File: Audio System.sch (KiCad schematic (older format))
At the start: 41 parts

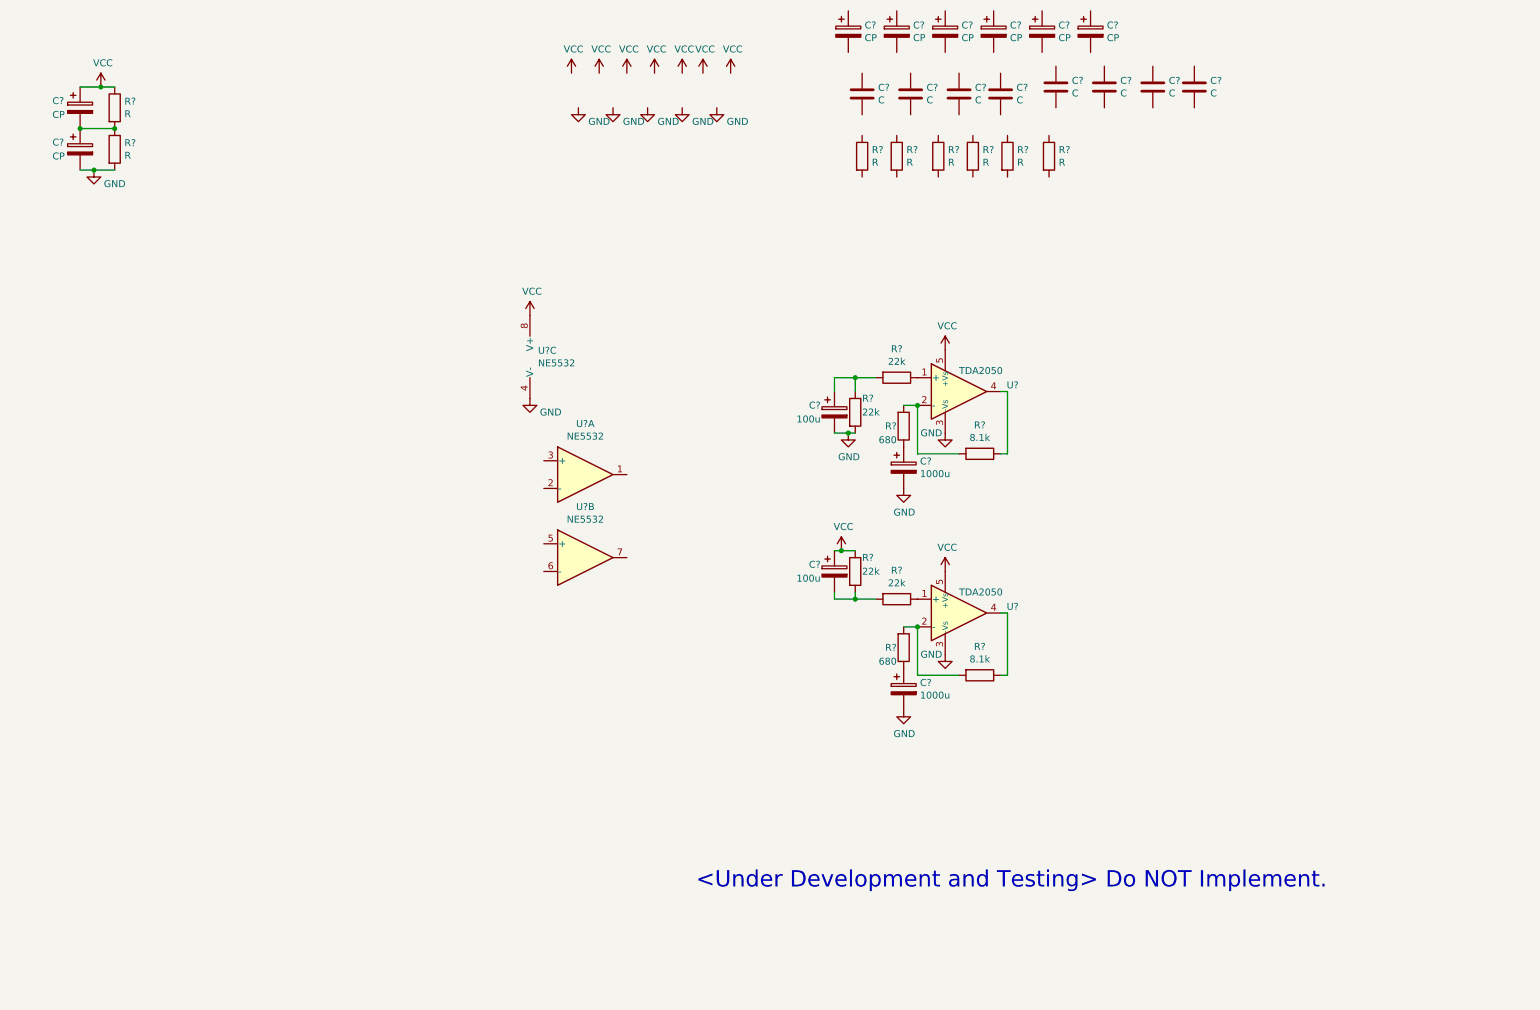
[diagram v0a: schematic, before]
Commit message: 0.2b
Power Amplifier Test 1 Complete
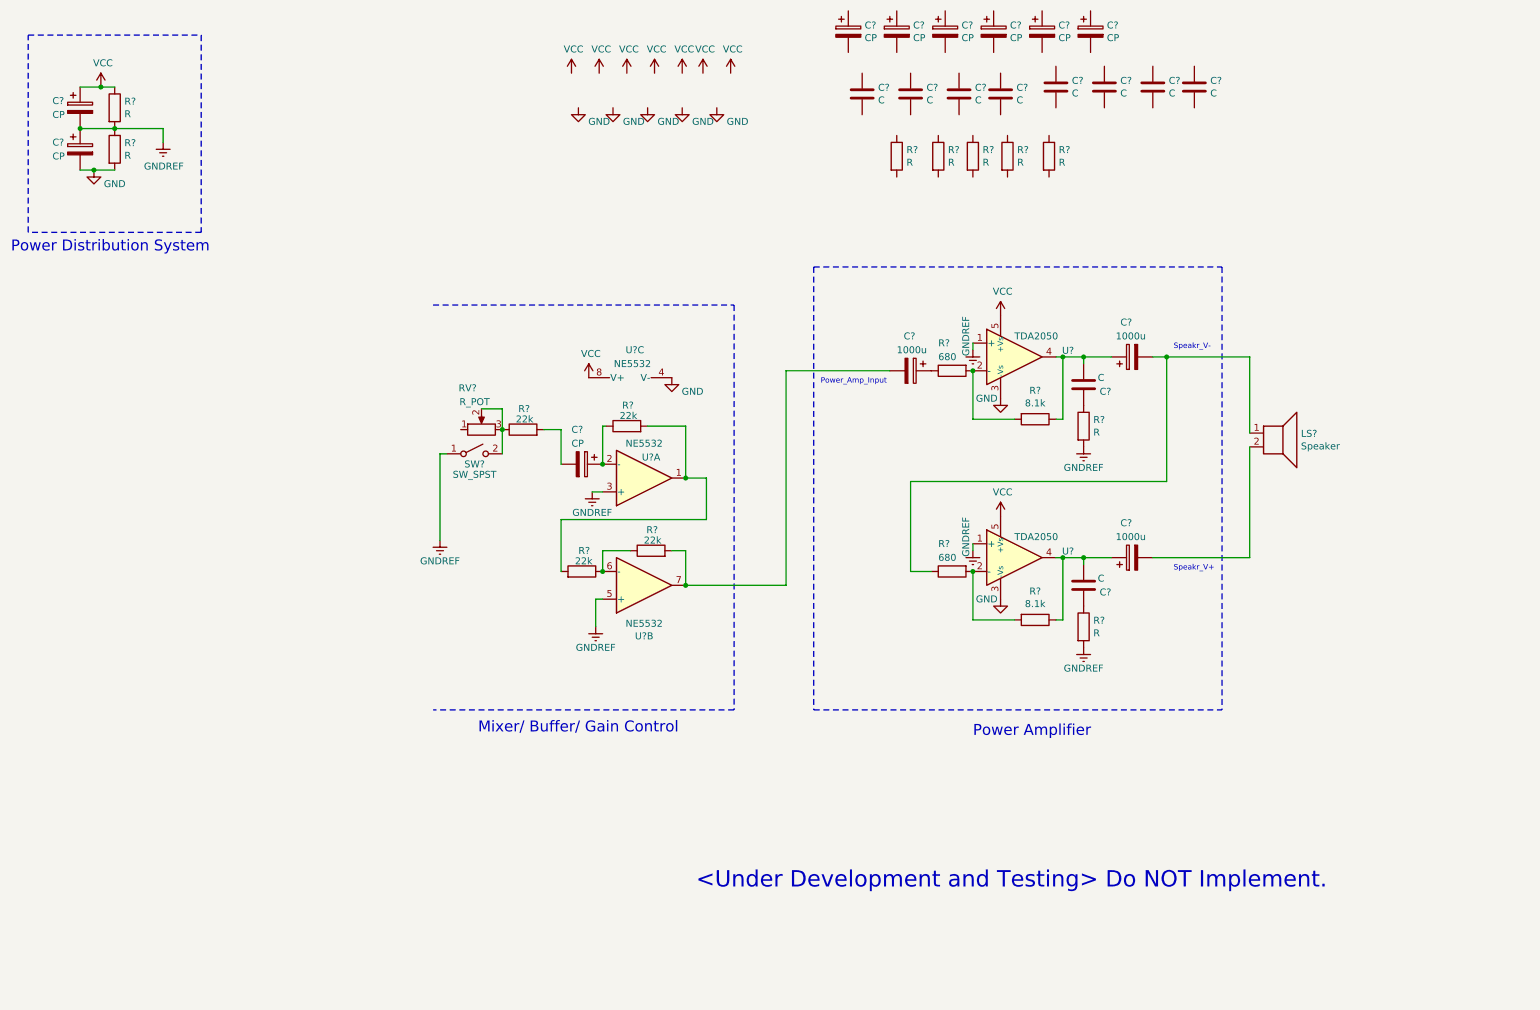
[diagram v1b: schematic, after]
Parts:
- removed C? (x2): 100u, symbol Device:CP
- removed C?: 1000u, symbol Device:CP
- removed R? (x4): 22k, symbol Device:R
- removed R?: 8.1k, symbol Device:R
- removed R?: 680, symbol Device:R
- removed U?: TDA2050, Package_TO_SOT_THT:TO-220-5_P3.4x3.7mm_StaggerOdd_Lead3.8mm_Vertical, symbol Amplifier_Audio:TDA2050
- added C? (x2): C, symbol Device:C
- added C? (x2): 1000u, symbol Device:CP
- added C?: CP, symbol Device:CP
- added LS?: Speaker, symbol Device:Speaker
- added R? (x2): R, symbol Device:R
- added R?: 8.1k, symbol Device:R
- added R?: 680, symbol Device:R
- added R? (x3): 22k, symbol Device:R
- added RV?: R_POT, symbol Device:R_POT
- added SW?: SW_SPST, symbol Switch:SW_SPST
- added U?: TDA2050, Package_TO_SOT_THT:TO-220-5_P3.4x3.7mm_StaggerOdd_Lead3.8mm_Vertical, symbol Amplifier_Audio:TDA2050
- R?: value R -> 22k
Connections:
- net GND: now also U?.3 (-Vs); no longer C?.2
- net VCC: now also U?.5 (+Vs)
- net GNDREF: now reaches U?.1 (+)
- net GNDREF: now also C?.1, C?.2, R?.1, R?.2, U?.3 (+), U?.5 (+), R?.2, R?.2, SW?.1 (A), U?.1 (+)
- net at R?.1, U?.4: now also C?.1, C?.2
- net at R?.1: now also U?.6 (-), R?.1
- net at R?.2: now also U?.1, R?.2
- net at U?.2 (-): now also C?.1, R?.1
- net at U?.7: now also C?.2, R?.2
- new net: C?.1, R?.1 (x2)
- new net: C?.2, LS?.1, R?.1
- new net: R?.2, R?.2, U?.2 (-)
- new net: C?.1, C?.2, R?.1, U?.4
- new net: C?.2, LS?.2
- new net: R?.1, RV?.2, RV?.3, SW?.2 (B)
- new net: C?.2, R?.2
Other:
- note added: "Mixer/ Buffer/ Gain Control"
- note added: "Power Amplifier"
- note added: "Power Distribution System"
- note added: "Power_Amp_Input"
- note added: "Speakr_V+"
- note added: "Speakr_V-"
- moved on the sheet: C?, R?, U?, U?A, U?B, U?C

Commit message: 0.3b
Input sources Preamp layout. Test Pending.
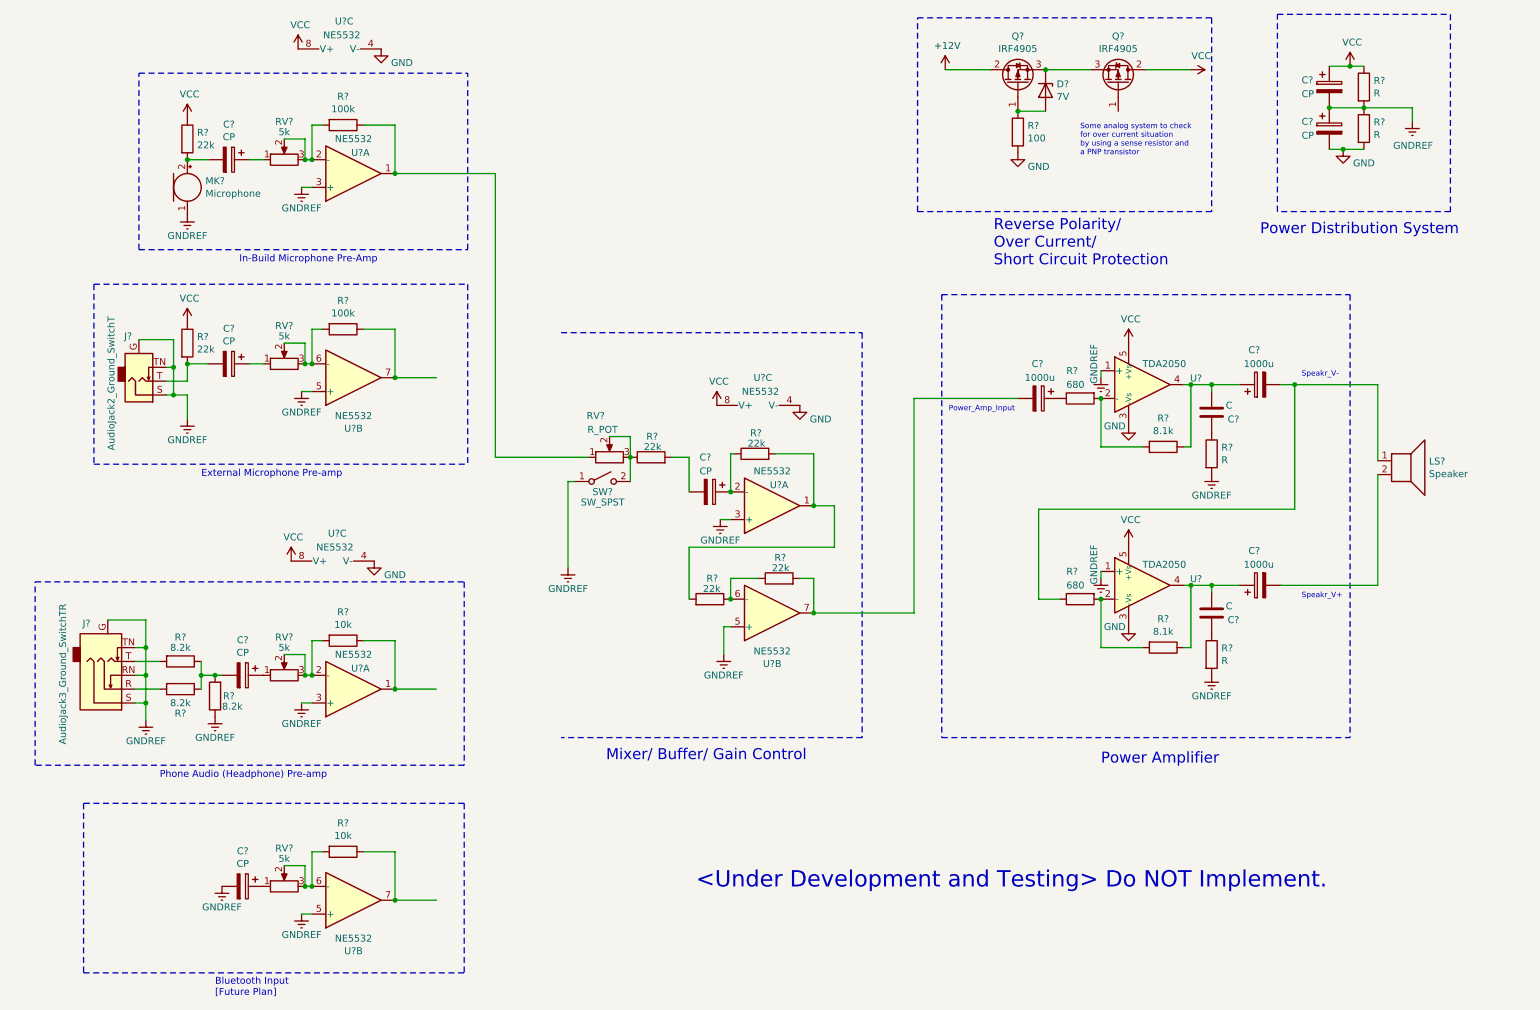
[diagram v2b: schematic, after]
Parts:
- removed C? (x8): C, symbol Device:C
- removed C? (x6): CP, symbol Device:CP
- removed R? (x5): R, symbol Device:R
- added C? (x4): CP, symbol Device:CP
- added D?: 7V, Diode_THT:D_DO-35_SOD27_P10.16mm_Horizontal, symbol Diode:ZPDxx
- added J?: AudioJack2_Ground_SwitchT, symbol Connector:AudioJack2_Ground_SwitchT
- added J?: AudioJack3_Ground_SwitchTR, symbol Connector:AudioJack3_Ground_SwitchTR
- added MK?: Microphone, symbol Device:Microphone
- added Q? (x2): IRF4905, Package_TO_SOT_THT:TO-220-3_Vertical, symbol Transistor_FET:IRF4905
- added R? (x2): 22k, symbol Device:R
- added R? (x2): 100k, symbol Device:R
- added R? (x2): 10k, symbol Device:R
- added R? (x3): 8.2k, symbol Device:R
- added R?: 100, symbol Device:R
- added RV? (x4): 5k, symbol Device:R_POT
- added U? (x6): NE5532, symbol Amplifier_Operational:NE5532
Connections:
- net GND: now also R?.2, U?.4 (V-), U?.4 (V-)
- net GNDREF: now also C?.2, J?.G, J?.G, J?.RN, J?.S, J?.S, J?.TN, J?.TN, MK?.1 (-), R?.1, U?.3 (+), U?.3 (+), U?.5 (+), U?.5 (+)
- net VCC: now also Q?.2 (D), R?.1, R?.1, U?.8 (V+), U?.8 (V+)
- net at RV?.1: now also R?.1, U?.1
- new net: R?.2, RV?.2, RV?.3, U?.2 (-) (x2)
- new net: R?.2, RV?.2, RV?.3, U?.6 (-) (x2)
- new net: R?.1, U?.7 (x2)
- new net: R?.1, U?.1
- new net: C?.2, MK?.2 (+), R?.2
- new net: C?.1, RV?.1 (x4)
- new net: C?.2, J?.T, R?.2
- new net: C?.2, R?.1, R?.1, R?.2
- new net: J?.R, R?.2
- new net: J?.T, R?.2
- new net: D?.2 (A), Q?.1 (G), R?.1
- new net: D?.1 (K), Q?.3 (S), Q?.3 (S)
- new net +12V: Q?.2 (D)
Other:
- note added: "Bluetooth Input\n[Future Plan]"
- note added: "External Microphone Pre-amp"
- note added: "In-Build Microphone Pre-Amp"
- note added: "Phone Audio (Headphone) Pre-amp"
- note added: "Reverse Polarity/ \nOver Current/ \nShort Circuit Protection"
- note added: "Some analog system to check\nfor over current situation\nby using a sense resistor and\na PNP transistor"
- moved on the sheet: C?, LS?, R?, RV?, SW?, U?, U?A, U?B, U?C

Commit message: Tested | Working | need to calcuulate RC filter values.
v1.1
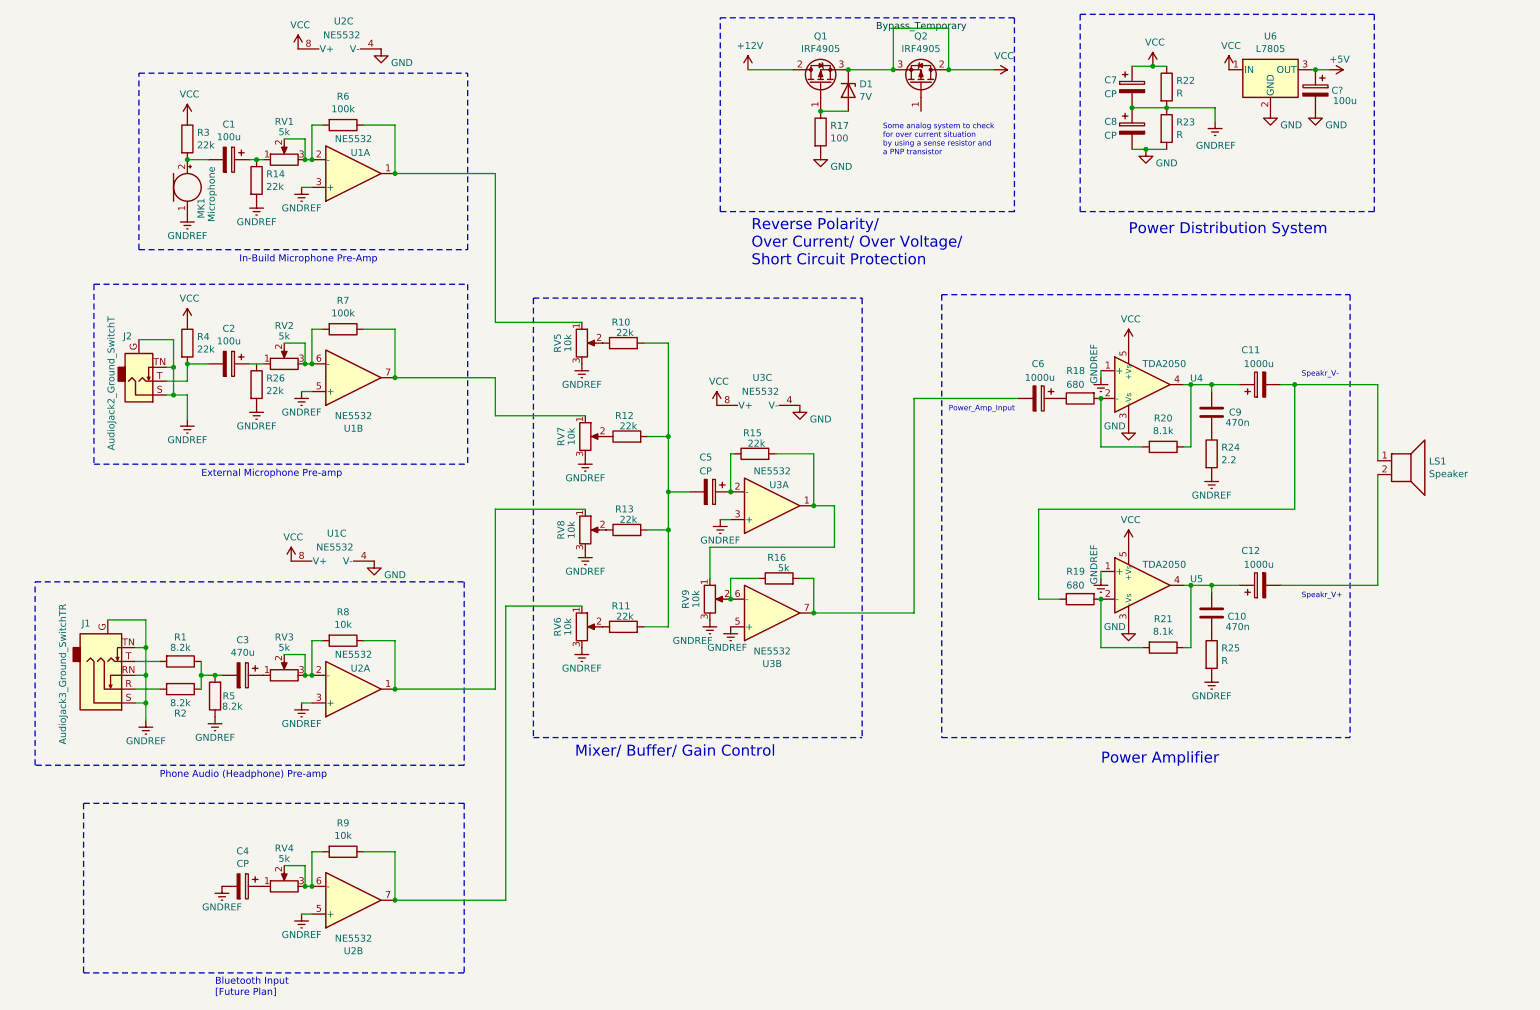
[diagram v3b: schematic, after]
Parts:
- removed R?: 22k, symbol Device:R
- removed SW?: SW_SPST, symbol Switch:SW_SPST
- added C?: 100u, symbol Device:CP
- added R10, R11, R13, R14, R26: 22k, symbol Device:R
- added RV5, RV6, RV8, RV9: 10k, symbol Device:R_POT
- added U6: L7805, symbol Regulator_Linear:L7805
- C1, C2: renamed from C?; value CP -> 100u
- C10, C9: renamed from C?; value C -> 470n
- C3: renamed from C?; value CP -> 470u
- R16: renamed from R?; value 22k -> 5k
- R24: renamed from R?; value R -> 2.2
- RV7: renamed from RV?; value R_POT -> 10k
- gave numbers to parts that had none: 42
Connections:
- net GND: now also C?.2, U6.2 (GND)
- net GNDREF: now also RV7.3, R14.2, R26.2, RV5.3, RV6.3, RV8.3, RV9.3
- net VCC: now also D1.1 (K), Q1.3 (S), Q2.3 (S), U6.1 (IN)
- net at C11.1, R20.1, U4.4: now also C9.1; no longer C9.2
- net at R16.1, U3.6 (-): now also RV9.2
- net at R15.2, U3.1: now also RV9.1
- net at R6.1, U1.1: now also RV5.1; no longer RV7.1
- net at R7.1, U1.7: now also RV7.1
- net at R8.1, U2.1: now also RV8.1
- net at R9.1, U2.7: now also RV6.1
- net at R24.1: now also C9.2; no longer C9.1
- net at C1.1, RV1.1: now also R14.1
- net at R12.1, RV7.2: no longer RV7.3
- net at C5.2, R12.2: now also R10.2, R11.2, R13.2
- new net: R13.1, RV8.2
- new net: R11.1, RV6.2
- new net: R10.1, RV5.2
- new net +5V: C?.1, U6.3 (OUT)
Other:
- note added: "Reverse Polarity/ \nOver Current/ Over Voltage/\nShort Circuit Protection"
- note removed: "<Under Development and Testing> Do NOT Implement."
- note removed: "Reverse Polarity/ \nOver Current/ \nShort Circuit Protection"
- moved on the sheet: C7, C8, D1, Q1, Q2, R12, R17, R22, R23, RV7
